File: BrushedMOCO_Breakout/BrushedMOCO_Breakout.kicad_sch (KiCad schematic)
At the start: 24 parts, among them Q1 Si4156DY, Q2 Si4156DY, Q3 Si4156DY, Q4 Si4156DY, U1 74LVC2G04, U2 IRS2308, U3 IRS2308

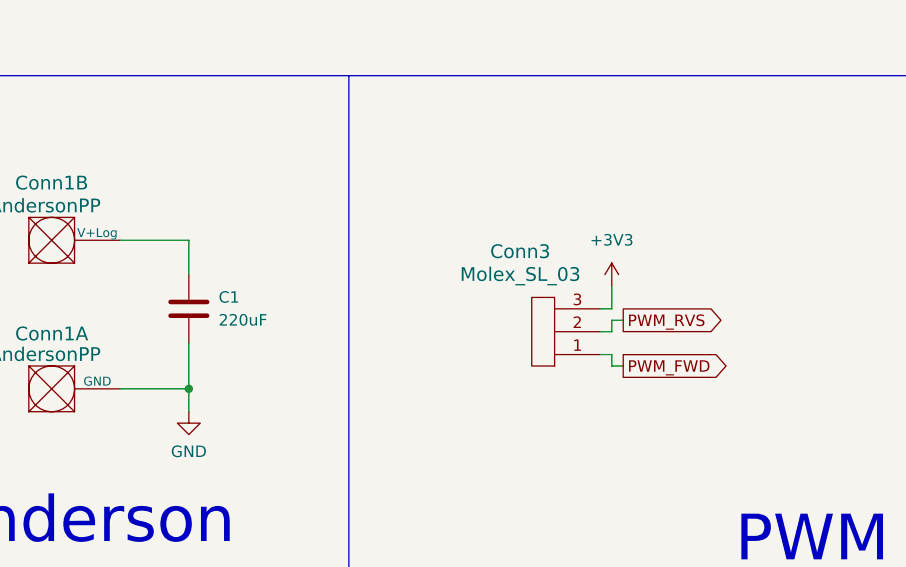
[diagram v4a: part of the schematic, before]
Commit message: A general outline of where stuff should go
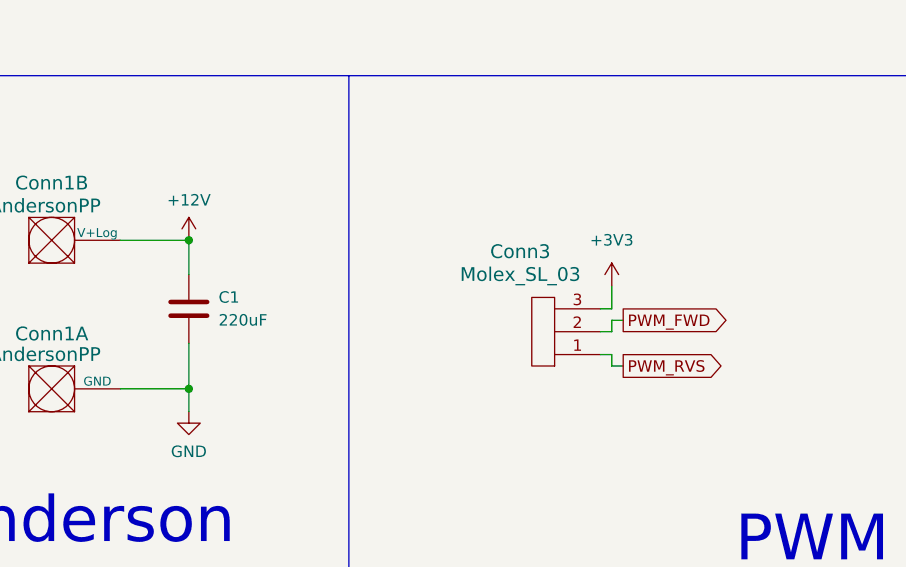
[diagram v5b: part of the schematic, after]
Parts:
- C1: footprint Capacitor_SMD:C_0603_1608Metric_Pad1.08x0.95mm_HandSolder -> Capacitor_THT:CP_Radial_D6.3mm_P2.50mm
- Conn1, Conn2: footprint MRDT_Connectors:Square_Anderson_2_H_Side_By_Side_PV -> MRDT_Connectors:Square_Anderson_2_H_Side_By_Side
- Conn3: footprint MRDT_Connectors:MOLEX_SL_03_Vertical -> MRDT_Connectors:MOLEX_SL_03_Horizontal
- U2, U3: footprint Package_SO:SOIC-8-1EP_3.9x4.9mm_P1.27mm_EP2.29x3mm -> Package_SO:SOIC-8_3.9x4.9mm_P1.27mm
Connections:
- net +12V: now also C1.2, Conn1.2 (V+Log)
- net PWM_FWD: now also Conn3.2; no longer Conn3.1
- net PWM_RVS: now also Conn3.1; no longer Conn3.2
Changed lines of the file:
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@@
   (junction (at 254 72.39) (diameter 0) (color 0 0 0 0)
   )
+  (junction (at 58.42 128.27) (diameter 0) (color 0 0 0 0)
+  )
   (junction (at 82.55 21.59) (diameter 0) (color 0 0 0 0)
   )
@@
     (stroke (width 0) (type default))
   )
+  (wire (pts (xy 105.41 137.16) (xy 106.68 137.16))
+    (stroke (width 0) (type default))
+  )
   (wire (pts (xy 218.44 46.99) (xy 205.74 46.99))
     (stroke (width 0) (type default))
@@
   )
   (wire (pts (xy 129.54 44.45) (xy 130.81 44.45))
-    (stroke (width 0) (type default))
-  )
-  (wire (pts (xy 105.41 137.16) (xy 106.68 137.16))
     (stroke (width 0) (type default))
   )
@@
     )
   )
+  (global_label "PWM_FWD" (shape output) (at 106.68 137.16 0) (fields_autoplaced)
+    (effects (font (size 1.27 1.27)) (justify left))
+    (property "Intersheetrefs" "${INTERSHEET_REFS}" (at 118.6156 137.16 0)
+      (effects (font (size 1.27 1.27)) (justify left) hide)
+    )
+  )
   (global_label "PWM_FWD" (shape input) (at 49.53 77.47 270) (fields_autoplaced)
     (effects (font (size 1.27 1.27)) (justify right))
@@
     )
   )
-  (global_label "PWM_RVS" (shape output) (at 106.68 137.16 0) (fields_autoplaced)
+  (global_label "PWM_RVS" (shape output) (at 106.68 142.24 0) (fields_autoplaced)
     (effects (font (size 1.27 1.27)) (justify left))
-    (property "Intersheetrefs" "${INTERSHEET_REFS}" (at 118.3737 137.16 0)
-      (effects (font (size 1.27 1.27)) (justify left) hide)
-    )
-  )
-  (global_label "PWM_FWD" (shape output) (at 106.68 142.24 0) (fields_autoplaced)
-    (effects (font (size 1.27 1.27)) (justify left))
-    (property "Intersheetrefs" "${INTERSHEET_REFS}" (at 118.6156 142.24 0)
+    (property "Intersheetrefs" "${INTERSHEET_REFS}" (at 118.3737 142.24 0)
       (effects (font (size 1.27 1.27)) (justify left) hide)
     )
@@
       (effects (font (size 1.27 1.27)) (justify right))
     )
-    (property "Footprint" "Capacitor_SMD:C_0603_1608Metric_Pad1.08x0.95mm_HandSolder" (at 57.4548 132.08 0)
+    (property "Footprint" "Capacitor_THT:CP_Radial_D6.3mm_P2.50mm" (at 57.4548 132.08 0)
       (effects (font (size 1.27 1.27)) hide)
     )
@@
       (effects (font (size 1.524 1.524)) (justify right))
     )
-    (property "Footprint" "MRDT_Connectors:Square_Anderson_2_H_Side_By_Side_PV" (at 144.78 27.94 0)
+    (property "Footprint" "MRDT_Connectors:Square_Anderson_2_H_Side_By_Side" (at 144.78 27.94 0)
       (effects (font (size 1.524 1.524)) hide)
     )
@@
       (effects (font (size 1.27 1.27)) (justify left))
     )
-    (property "Footprint" "Package_SO:SOIC-8-1EP_3.9x4.9mm_P1.27mm_EP2.29x3mm" (at 226.06 39.37 0)
+    (property "Footprint" "Package_SO:SOIC-8_3.9x4.9mm_P1.27mm" (at 226.06 39.37 0)
       (effects (font (size 1.27 1.27) italic) hide)
     )
@@
       (effects (font (size 1.524 1.524)))
     )
-    (property "Footprint" "MRDT_Connectors:Square_Anderson_2_H_Side_By_Side_PV" (at 151.13 60.96 0)
+    (property "Footprint" "MRDT_Connectors:Square_Anderson_2_H_Side_By_Side" (at 151.13 60.96 0)
       (effects (font (size 1.524 1.524)) hide)
     )
@@
       (effects (font (size 1.27 1.27)) (justify left))
     )
-    (property "Footprint" "Package_SO:SOIC-8-1EP_3.9x4.9mm_P1.27mm_EP2.29x3mm" (at 71.12 39.37 0)
+    (property "Footprint" "Package_SO:SOIC-8_3.9x4.9mm_P1.27mm" (at 71.12 39.37 0)
       (effects (font (size 1.27 1.27) italic) hide)
     )
@@
       (effects (font (size 1.524 1.524)))
     )
-    (property "Footprint" "MRDT_Connectors:MOLEX_SL_03_Vertical" (at 99.06 134.62 0)
+    (property "Footprint" "MRDT_Connectors:MOLEX_SL_03_Horizontal" (at 99.06 134.62 0)
       (effects (font (size 1.524 1.524)) hide)
     )
@@
         (path "/09f10023-b6cf-44c5-8847-9c4a76610e70"
           (reference "Conn3") (unit 1)
+        )
+      )
+    )
+  )
+  (symbol (lib_id "power:+12V") (at 58.42 128.27 0) (unit 1)
+    (in_bom yes) (on_board yes) (dnp no) (fields_autoplaced)
+    (property "Reference" "#PWR05" (at 58.42 132.08 0)
+      (effects (font (size 1.27 1.27)) hide)
+    )
+    (property "Value" "+12V" (at 58.42 123.825 0)
+      (effects (font (size 1.27 1.27)))
+    )
+    (property "Footprint" "" (at 58.42 128.27 0)
+      (effects (font (size 1.27 1.27)) hide)
+    )
+    (property "Datasheet" "" (at 58.42 128.27 0)
+      (effects (font (size 1.27 1.27)) hide)
+    )
+    (pin "1")
+    (instances
+      (project "BrushedMOCO_Breakout"
+        (path "/09f10023-b6cf-44c5-8847-9c4a76610e70"
+          (reference "#PWR05") (unit 1)
         )
       )
@@
       (effects (font (size 1.524 1.524)))
     )
-    (property "Footprint" "MRDT_Connectors:Square_Anderson_2_H_Side_By_Side_PV" (at 36.83 144.78 0)
+    (property "Footprint" "MRDT_Connectors:Square_Anderson_2_H_Side_By_Side" (at 36.83 144.78 0)
       (effects (font (size 1.524 1.524)) hide)
     )
@@
       (effects (font (size 1.524 1.524)))
     )
-    (property "Footprint" "MRDT_Connectors:Square_Anderson_2_H_Side_By_Side_PV" (at 36.83 161.29 0)
+    (property "Footprint" "MRDT_Connectors:Square_Anderson_2_H_Side_By_Side" (at 36.83 161.29 0)
       (effects (font (size 1.524 1.524)) hide)
     )

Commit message: Finish layout for order
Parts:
- R1, R6: value 120 -> 100
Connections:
- net +12V: now also C1.1; no longer C1.2
- net GND: now also C1.2; no longer C1.1
- net PWM_FWD: now also D1.2 (A), U2.2 (HIN); no longer U2.3 (LIN)
- net PWM_RVS: now also D4.2 (A), U3.2 (HIN); no longer U3.3 (LIN)
- net at C2.1, D2.1 (K), U2.8 (VB): no longer R2.1, U2.7 (HO)
- net at C4.1, D3.1 (K), U3.8 (VB): no longer R4.1, U3.7 (HO)
- new net: U1.6, U2.3 (LIN)
- new net: R4.1, U3.7 (HO)
- new net: R2.1, U2.7 (HO)
- new net: U1.4, U3.3 (LIN)
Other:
- note added: "PWM Signals"
- note added: "Power"
- note removed: "Anderson"
- note removed: "Diode Power"
- note removed: "PWM"
- moved on the sheet: C1, C2, C3, C4, Conn1A, Conn1B, Conn2A, Conn2B, Conn3, D1, D2, D3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
